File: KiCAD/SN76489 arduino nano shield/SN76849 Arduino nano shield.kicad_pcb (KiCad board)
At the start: 2 copper layers, 68.2 x 67 mm, 17 parts, among them J1 Arduino_in, J2 audio_debug, J3 OLED_wit, J4 I2C_in, J6 gat1, J7 gat2, J8 geluid_uit, U1 PCF8574, U2 LM358, U3 SN76489

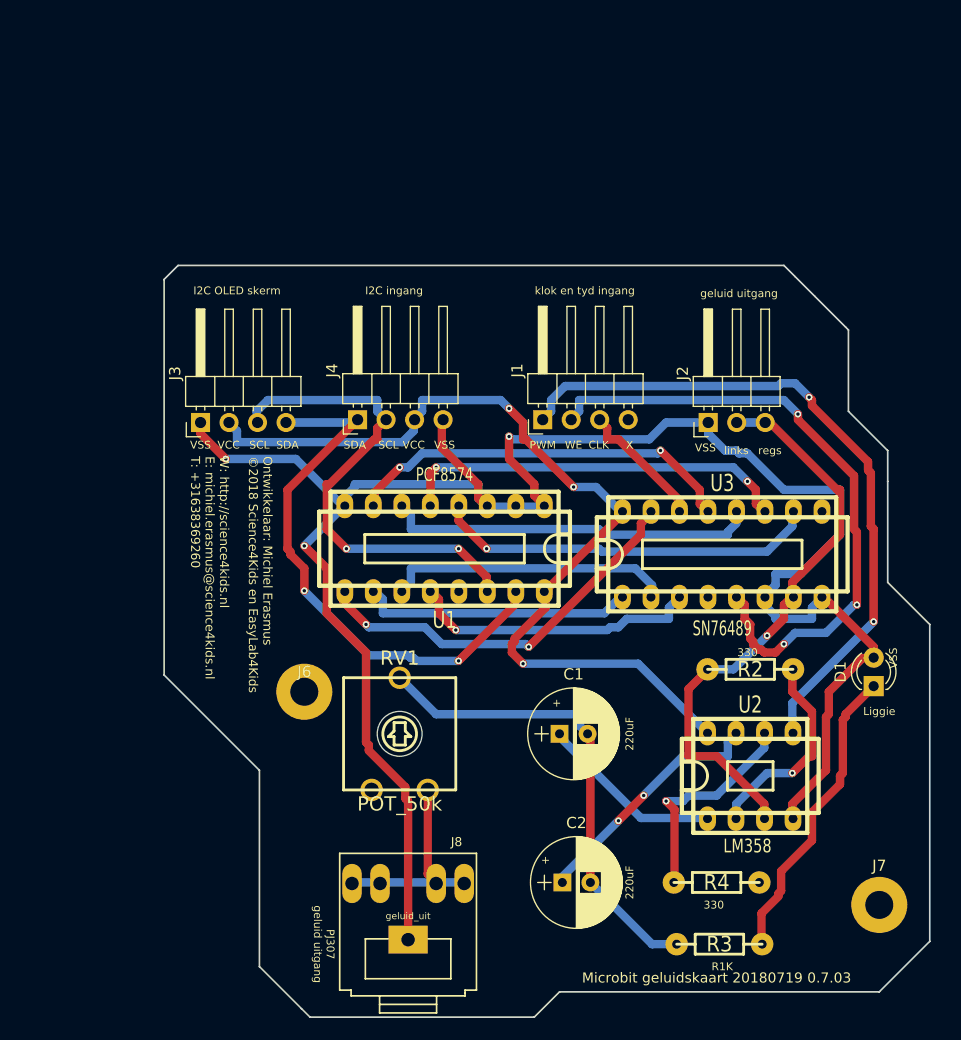
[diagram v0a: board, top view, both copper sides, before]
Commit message: versie 20180905 0.7.06
LM358 opAmp wasverwyderd,
Dip-14 Xtal clock 4Mhz toegevoegd.
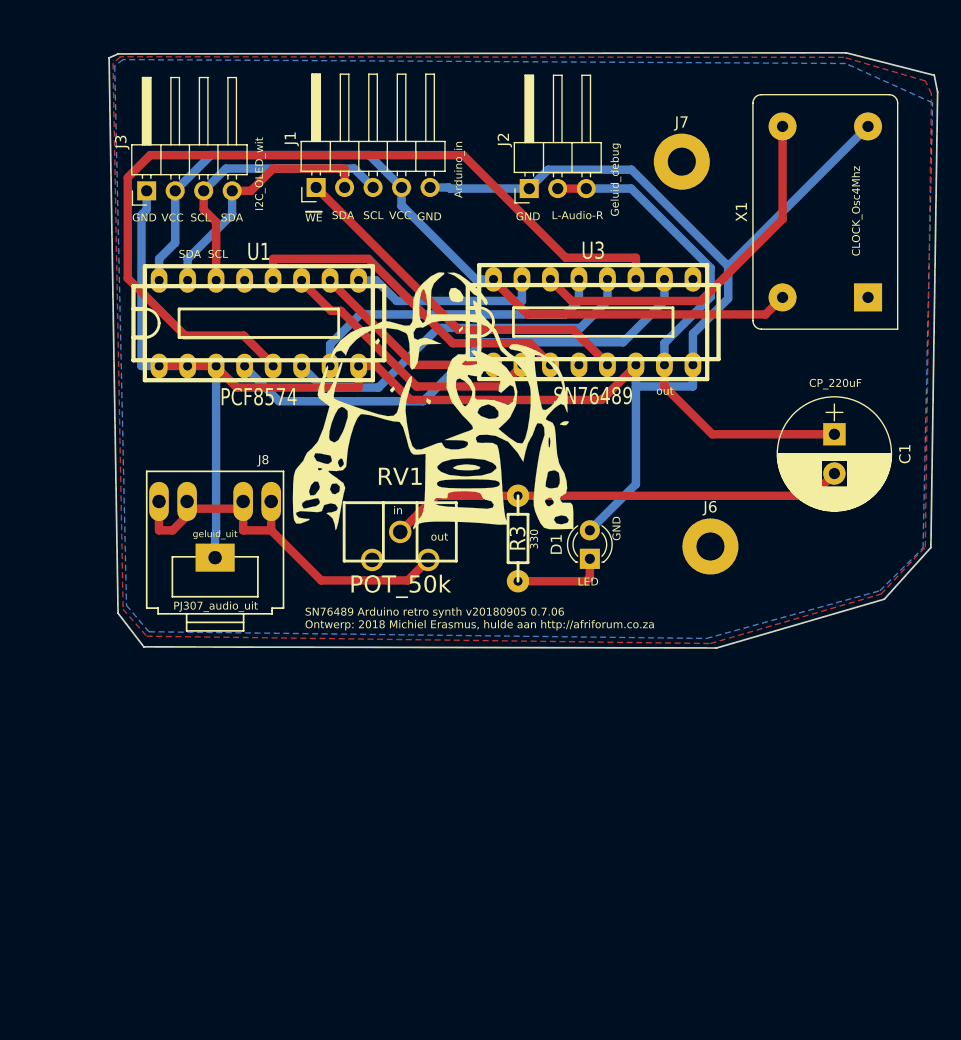
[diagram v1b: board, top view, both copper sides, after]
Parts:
- removed C2: CP_220uF, Capacitors_THT:CP_Radial_D8.0mm_P2.50mm
- removed J4: I2C_in, Pin_Headers:Pin_Header_Angled_1x04_Pitch2.54mm
- removed R2, R4: 330, w_pth_resistors:RC03
- removed U2: LM358, w_pth_circuits:dil_8-300_socket
- added J5: LOGO, lib_michiel:Sovjet_simpits_logo01, F.Cu at (63.3, 53.6)
- added X1: CLK_DIP14_4Mhz, Oscillators:Oscillator_DIP-14_LargePads, F.Cu at (102.0, 44.6)
- C1: footprint Capacitors_THT:CP_Radial_D8.0mm_P2.50mm -> Capacitors_THT:CP_Radial_D10.0mm_P3.50mm
- J1: footprint Pin_Headers:Pin_Header_Angled_1x04_Pitch2.54mm -> Pin_Headers:Pin_Header_Angled_1x05_Pitch2.54mm
- RV1: footprint w_pth_resistors:trimmer_ecp_ca9-v10 -> w_pth_resistors:trimmer_ecp_ca9-h2,5
- moved J7 68.5 mm to (85.4, 32.5)
- moved R3 40.4 mm to (70.8, 66.1), turned to 90 degrees
- moved J6 38.4 mm to (88.0, 66.8)
- moved J8 38.1 mm to (43.8, 66.2)
- moved C1 36.2 mm to (99.0, 56.8), turned to 270 degrees
- moved J1 28.9 mm to (52.8, 34.8)
- moved D1 27.7 mm to (77.2, 67.9)
- moved J2 26.3 mm to (71.8, 34.9)
- moved U1 26.0 mm to (47.7, 46.9), turned to 0 degrees
- moved U3 23.7 mm to (77.5, 46.8)
- moved J3 21.2 mm to (37.7, 35.1)
- moved RV1 18.0 mm to (60.3, 65.5)
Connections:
- C1 pad 1: Net-(C1-Pad1) -> /Audio
- J1 pad 1: /PWM -> /~WE
- J1 pad 2: /WE -> /SDA
- J1 pad 3: /Clock -> /SCL
- J1 pad 4: (no net) -> /VCC
- J6 pad 1: (no net) -> Net-(J6-Pad1)
- J7 pad 1: (no net) -> Net-(J7-Pad1)
- RV1 pad 1: (no net) -> Net-(RV1-Pad1)
- U1 pad 13: (no net) -> Net-(U1-Pad13)
- U3 pad 4: (no net) -> Net-(U3-Pad4)
- U3 pad 5: /WE -> /~WE
- U3 pad 9: (no net) -> Net-(U3-Pad9)
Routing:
- net /PWM: track 61.7 -> 0.00 mm, vias 2 -> 0
- net /WE: track 57.5 -> 0.00 mm, vias 3 -> 0
- net /P1: track 35.4 -> 77.1 mm, vias 2 -> 0
- net /~WE: track 0.00 -> 32.6 mm
- net /SDA: track 49.7 -> 22.1 mm, vias 2 -> 0
- net Net-(C2-Pad1): track 22.1 -> 0.00 mm, vias 2 -> 0
- net /Clock: track 12.0 -> 32.8 mm
- net Net-(R4-Pad1): track 19.7 -> 0.00 mm, vias 1 -> 0
- net Net-(D1-Pad1): track 27.2 -> 8.19 mm
- net /SCL: track 43.9 -> 25.1 mm, vias 2 -> 0
- net /P4: track 36.0 -> 17.2 mm, vias 2 -> 0
- net Net-(R2-Pad1): track 18.4 -> 0.00 mm, vias 1 -> 0
- net Net-(J8-Pad2): track 19.2 -> 36.2 mm
- net Net-(C1-Pad1): track 16.6 -> 0.00 mm
- net GND: track 180.2 -> 164.4 mm, vias 3 -> 0
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- added copper zone on B.Cu, net GND
- added copper zone on F.Cu, net GND
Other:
- board size 68.2 x 67 mm -> 73.8 x 53 mm
- board text added: "Arduino_in"
- board text added: "CLOCK_Osc4Mhz"
- board text added: "CP_220uF"
- board text added: "GND"
- board text added: "Geluid_debug"
- board text added: "I2C_OLED_wit"
- board text added: "L-Audio-R"
- board text added: "LED"
- board text added: "PJ307_audio_uit"
- board text added: "SN76489 Arduino retro synth v20180905 0.7.06 Ontwerp: 2018 Michiel Erasmus, hulde aan http://afriforum.co.za"
- board text added: "in"
- board text added: "out"
- board text added: "~WE"
- board text removed: "+"
- board text removed: "220uF"
- board text removed: "CLK"
- board text removed: "I2C OLED skerm"
- board text removed: "I2C ingang"
- board text removed: "Liggie"
- board text removed: "Microbit geluidskaart 20180719 0.7.03"
- board text removed: "Ontwikkelaar: Michiel Erasmus ©2018 Science4Kids en EasyLab4Kids W: http://science4kids.nl E: michiel.erasmus@science4kids.nl T: +31638369260"
- board text removed: "PJ307 geluid uitgang"
- board text removed: "PWM"
- board text removed: "R1K"
- board text removed: "VSS"
- board text removed: "WE"
- board text removed: "X"
- board text removed: "geluid uitgang"
- board text removed: "klok en tyd ingang"
- board text removed: "links"
- board text removed: "regs"

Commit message: versie 20180905 0.7.06
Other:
- board size 73.8 x 53 mm -> 74 x 52.9 mm
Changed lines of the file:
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@@
   (general
     (thickness 1.6)
-    (drawings 36)
+    (drawings 38)
     (tracks 150)
     (zones 0)
@@
     )
   )
+  (gr_line (start 34.25 71.3) (end 34.25 71.6) (layer Edge.Cuts) (width 0.15))
+  (gr_line (start 35.15 72.75) (end 34.25 71.6) (layer Edge.Cuts) (width 0.15))
+  (gr_line (start 34.3 23.25) (end 34.25 71.3) (layer Edge.Cuts) (width 0.15))
+  (gr_line (start 106.5 75.85) (end 108.2 74.95) (layer Edge.Cuts) (width 0.2))
+  (gr_line (start 108.2 71.55) (end 108.2 74.95) (layer Edge.Cuts) (width 0.2))
+  (gr_line (start 88.5 75.85) (end 106.45 75.85) (layer Edge.Cuts) (width 0.2))
+  (gr_line (start 108.1 24.4) (end 108.2 71.6) (layer Edge.Cuts) (width 0.2))
+  (gr_line (start 106.65 22.9) (end 108.1 24.4) (layer Edge.Cuts) (width 0.2))
+  (gr_line (start 35.15 22.9) (end 106.65 22.9) (layer Edge.Cuts) (width 0.2))
   (gr_line (start 34.35 23.25) (end 35.15 22.9) (layer Edge.Cuts) (width 0.15))
-  (gr_line (start 35.15 72.75) (end 34.35 23.25) (layer Edge.Cuts) (width 0.15))
   (gr_line (start 37.45 75.75) (end 35.15 72.75) (layer Edge.Cuts) (width 0.15))
   (gr_line (start 88.5 75.85) (end 37.45 75.75) (layer Edge.Cuts) (width 0.15))
-  (gr_line (start 103.45 71.5) (end 88.5 75.85) (layer Edge.Cuts) (width 0.15))
-  (gr_line (start 107.6 66.9) (end 103.45 71.5) (layer Edge.Cuts) (width 0.15))
-  (gr_line (start 108.2 26.3) (end 107.6 66.9) (layer Edge.Cuts) (width 0.15))
-  (gr_line (start 107.9 24.8) (end 108.2 26.3) (layer Edge.Cuts) (width 0.15))
-  (gr_line (start 100.05 22.8) (end 107.9 24.8) (layer Edge.Cuts) (width 0.15))
-  (gr_line (start 35.15 22.9) (end 100.05 22.8) (layer Edge.Cuts) (width 0.15))
   (gr_text 330 (at 72.25 66.15 90) (layer F.SilkS)
     (effects (font (size 0.7 0.7) (thickness 0.175)))
@@
     (polygon
       (pts
-        (xy 34.7 23.75) (xy 35.6 72.4) (xy 37.7 74.8) (xy 87.95 75.45) (xy 103.15 71.05)
-        (xy 107.1 66.85) (xy 107.65 26.45) (xy 107.1 25.3) (xy 99.85 23.2) (xy 35.35 23.15)
+        (xy 108.05 74.8) (xy 106.4 75.65) (xy 37.8 75.4) (xy 34.6 71.2) (xy 34.5 23.35)
+        (xy 35.15 23.1) (xy 106.45 23.15) (xy 107.75 24.35)
       )
     )
@@
     (polygon
       (pts
-        (xy 34.85 23.95) (xy 35.9 72.05) (xy 37.9 74.4) (xy 87.6 75) (xy 103.05 70.75)
-        (xy 106.9 66.95) (xy 107.75 27.25) (xy 100 23.75) (xy 35.6 23.4)
+        (xy 106.25 23.35) (xy 35.15 23.3) (xy 34.6 23.55) (xy 34.9 71.1) (xy 38 75.2)
+        (xy 106.25 75.35) (xy 107.45 74.55) (xy 107.6 24.4)
       )
     )

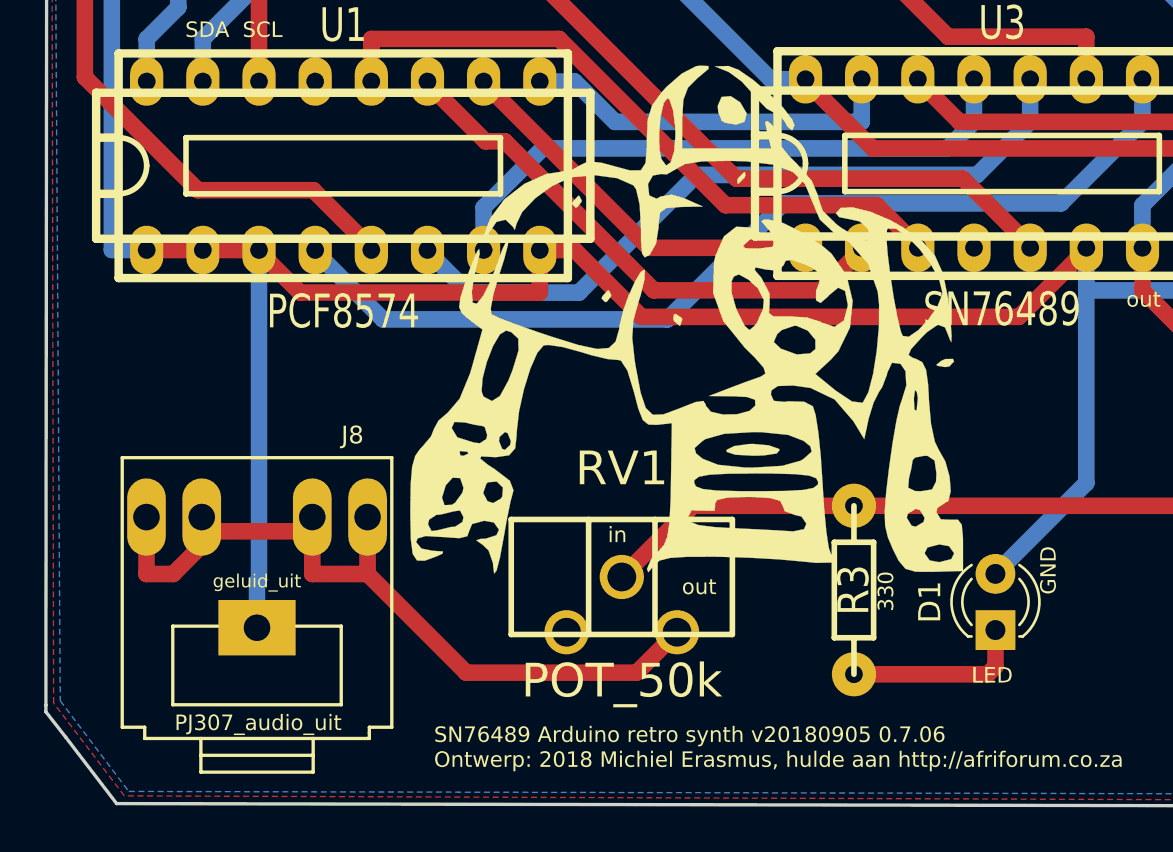
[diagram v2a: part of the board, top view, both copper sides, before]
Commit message: Bijgewerkt naar KiCAD 7.0
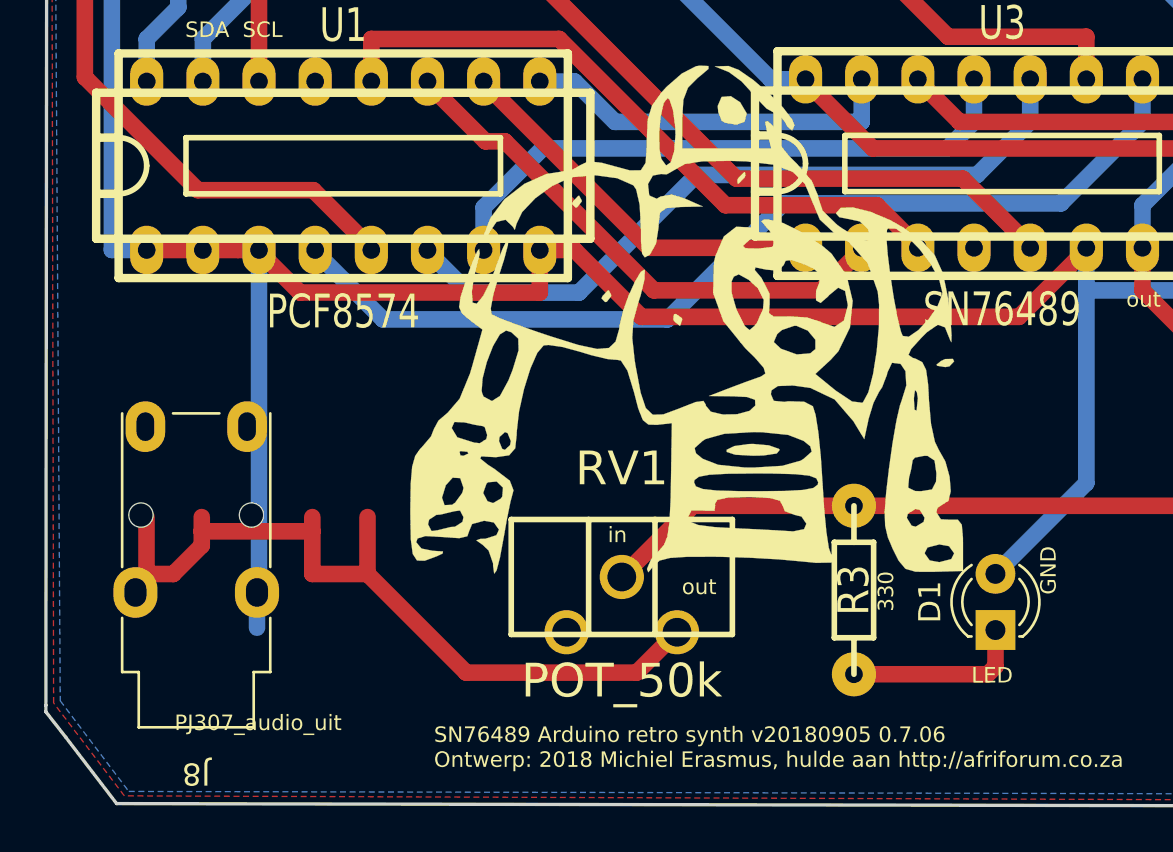
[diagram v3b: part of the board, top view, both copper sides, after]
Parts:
- J8: footprint lib_michiel:3.5mm_stereo_TRS_jack_A-853_Tayda_ -> Connector_Audio:Jack_3.5mm_Lumberg_1503_07_Horizontal
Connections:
- net /~WE renamed /~{WE}
- J6 pad 1: Net-(J6-Pad1) -> unconnected-(J6-Pin_1-Pad1)
- J7 pad 1: Net-(J7-Pad1) -> unconnected-(J7-Pin_1-Pad1)
- RV1 pad 1: Net-(RV1-Pad1) -> unconnected-(RV1-Pad1)
- U1 pad 13: Net-(U1-Pad13) -> unconnected-(U1-~{INT}-Pad13)
- U3 pad 4: Net-(U3-Pad4) -> unconnected-(U3-READY-Pad4)
- U3 pad 9: Net-(U3-Pad9) -> unconnected-(U3-N.C.-Pad9)
- X1 pad 1: Net-(X1-Pad1) -> unconnected-(X1-EN-Pad1)
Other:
- net class Default removed
- net class DityPCBs laat maak removed
- board text added: "~{WE}"
- board text removed: "~WE"

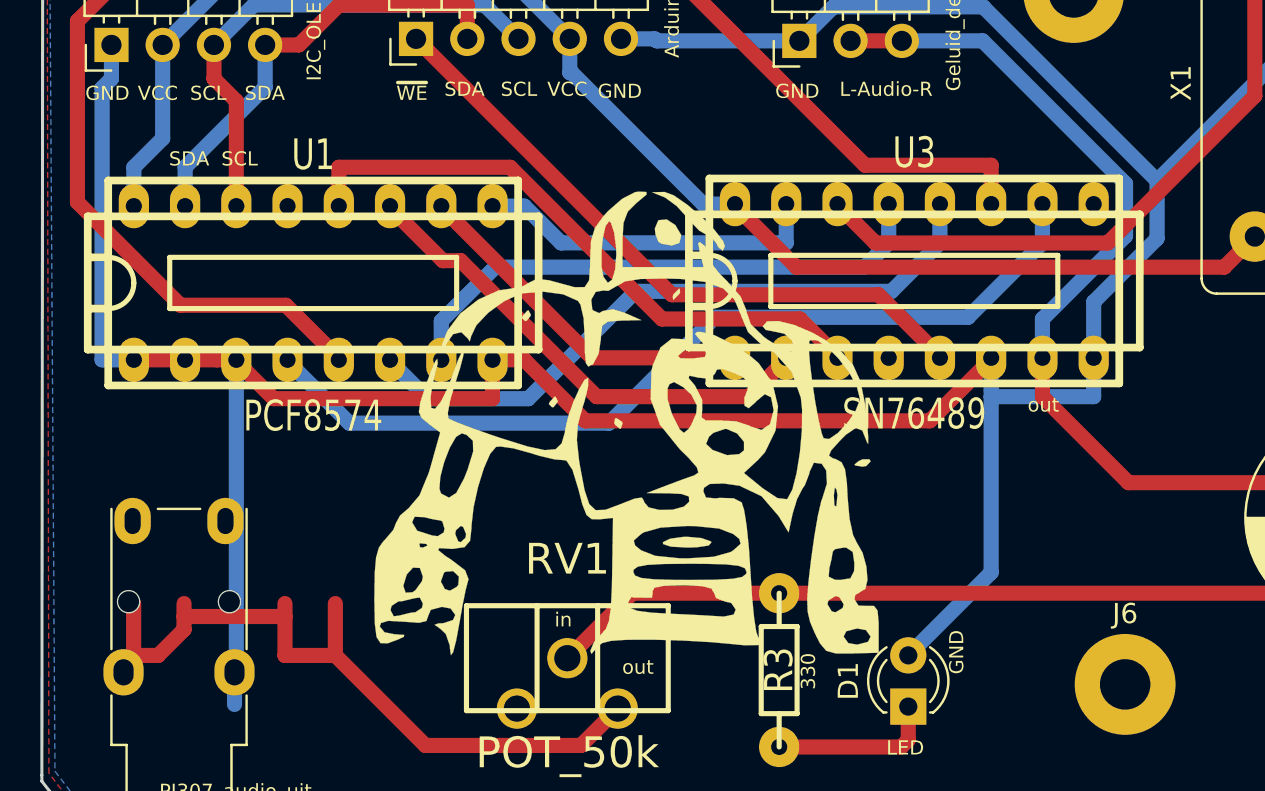
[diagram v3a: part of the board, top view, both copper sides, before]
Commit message: Bijgewerkt naar KiCAD 7.0
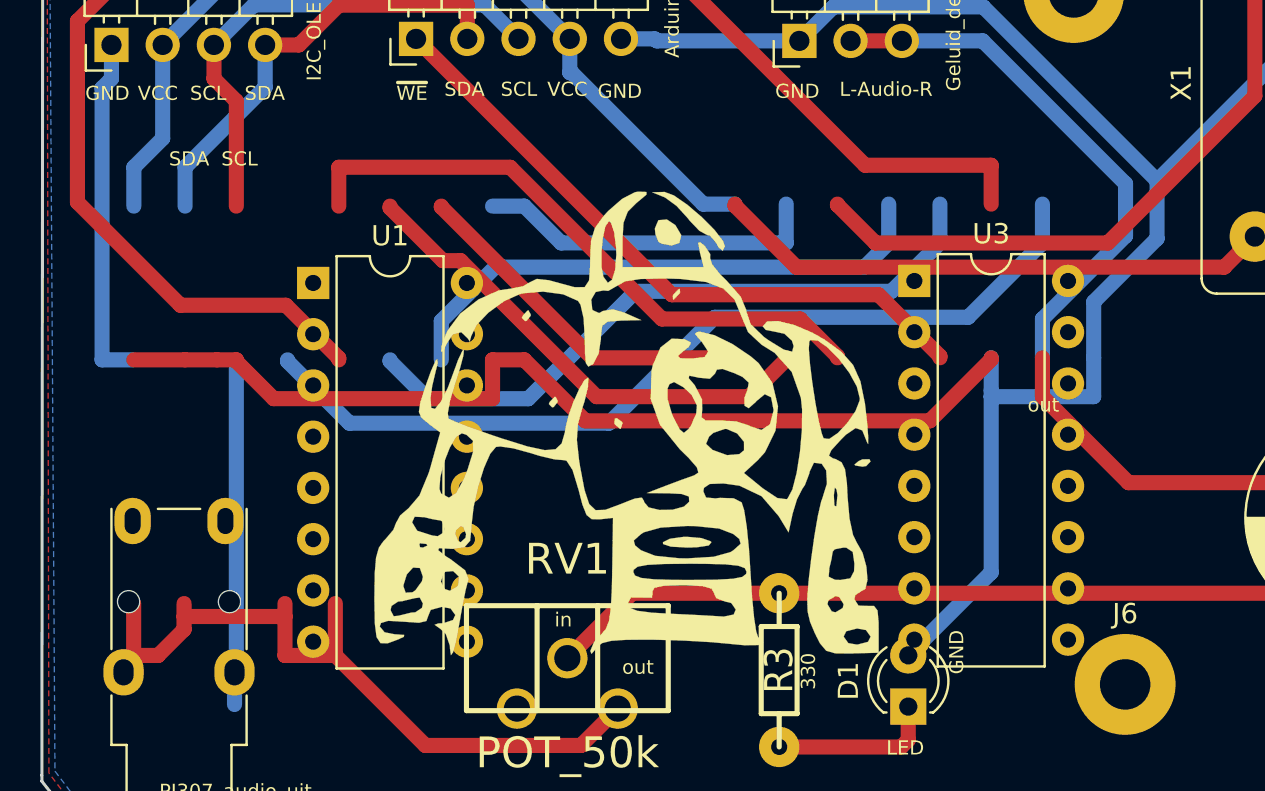
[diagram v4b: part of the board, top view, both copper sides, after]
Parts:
- U1, U3: footprint w_pth_circuits:dil_16-300_socket -> Package_DIP:DIP-16_W7.62mm
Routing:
- net GND: track 164.4 -> 241.5 mm
- net /P1: track 77.1 -> 0.00 mm
- net /VCC: track 71.6 -> 123.7 mm
- net /P3: track 27.6 -> 0.00 mm
- net /P6: track 24.4 -> 0.00 mm

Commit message: Bijgewerkt naar KiCAD 7.0
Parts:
- J1: footprint Pin_Headers:Pin_Header_Angled_1x05_Pitch2.54mm -> Connector_PinHeader_2.54mm:PinHeader_1x05_P2.54mm_Horizontal
- J2: footprint Pin_Headers:Pin_Header_Angled_1x03_Pitch2.54mm -> Connector_PinHeader_2.54mm:PinHeader_1x03_P2.54mm_Vertical
- J3: footprint Pin_Headers:Pin_Header_Angled_1x04_Pitch2.54mm -> Connector_PinHeader_2.54mm:PinHeader_1x04_P2.54mm_Horizontal

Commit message: Bijgewerkt naar KiCAD 7.0
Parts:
- removed J1: Arduino_in, Connector_PinHeader_2.54mm:PinHeader_1x05_P2.54mm_Horizontal
- removed X1: CLK_DIP14_4Mhz, Oscillators:Oscillator_DIP-14_LargePads
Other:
- board text added: "SN76489 Arduino retro synth v20180905 0.8 Ontwerp: 2023 Michiel Erasmus, hulde aan http://afriforum.co.za"
- board text removed: "CLOCK_Osc4Mhz"
- board text removed: "SN76489 Arduino retro synth v20180905 0.7.06 Ontwerp: 2018 Michiel Erasmus, hulde aan http://afriforum.co.za"
